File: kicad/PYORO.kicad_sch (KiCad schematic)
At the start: 113 parts, among them J1 BM06B-SRSS-TBLFSN, J2 Conn_01x04_Pin, J3 BM06B-SRSS-TBLFSN, J4 Conn_01x04_Pin, Q1 TEFT4300, Q2 TEFT4300, Q3 TEFT4300, Q4 TEFT4300, Q5 NMOS, Q6 NMOS, Q7 NMOS, Q8 NMOS, Q9 NMOS, SW1 SW_Push_Dual_x2, SW2 SW_Push_Dual_x2, U1 STM32H503CBTx, U10 UCC27524, U3 ICM-20948, U4 MC78LC18NTR, U5 LM1085-5.0, U6 AP2210N-3.3TRG1, U7 UCC27524, U8 ZXMHC3F381N8TC, U9 ZXMHC3F381N8TC

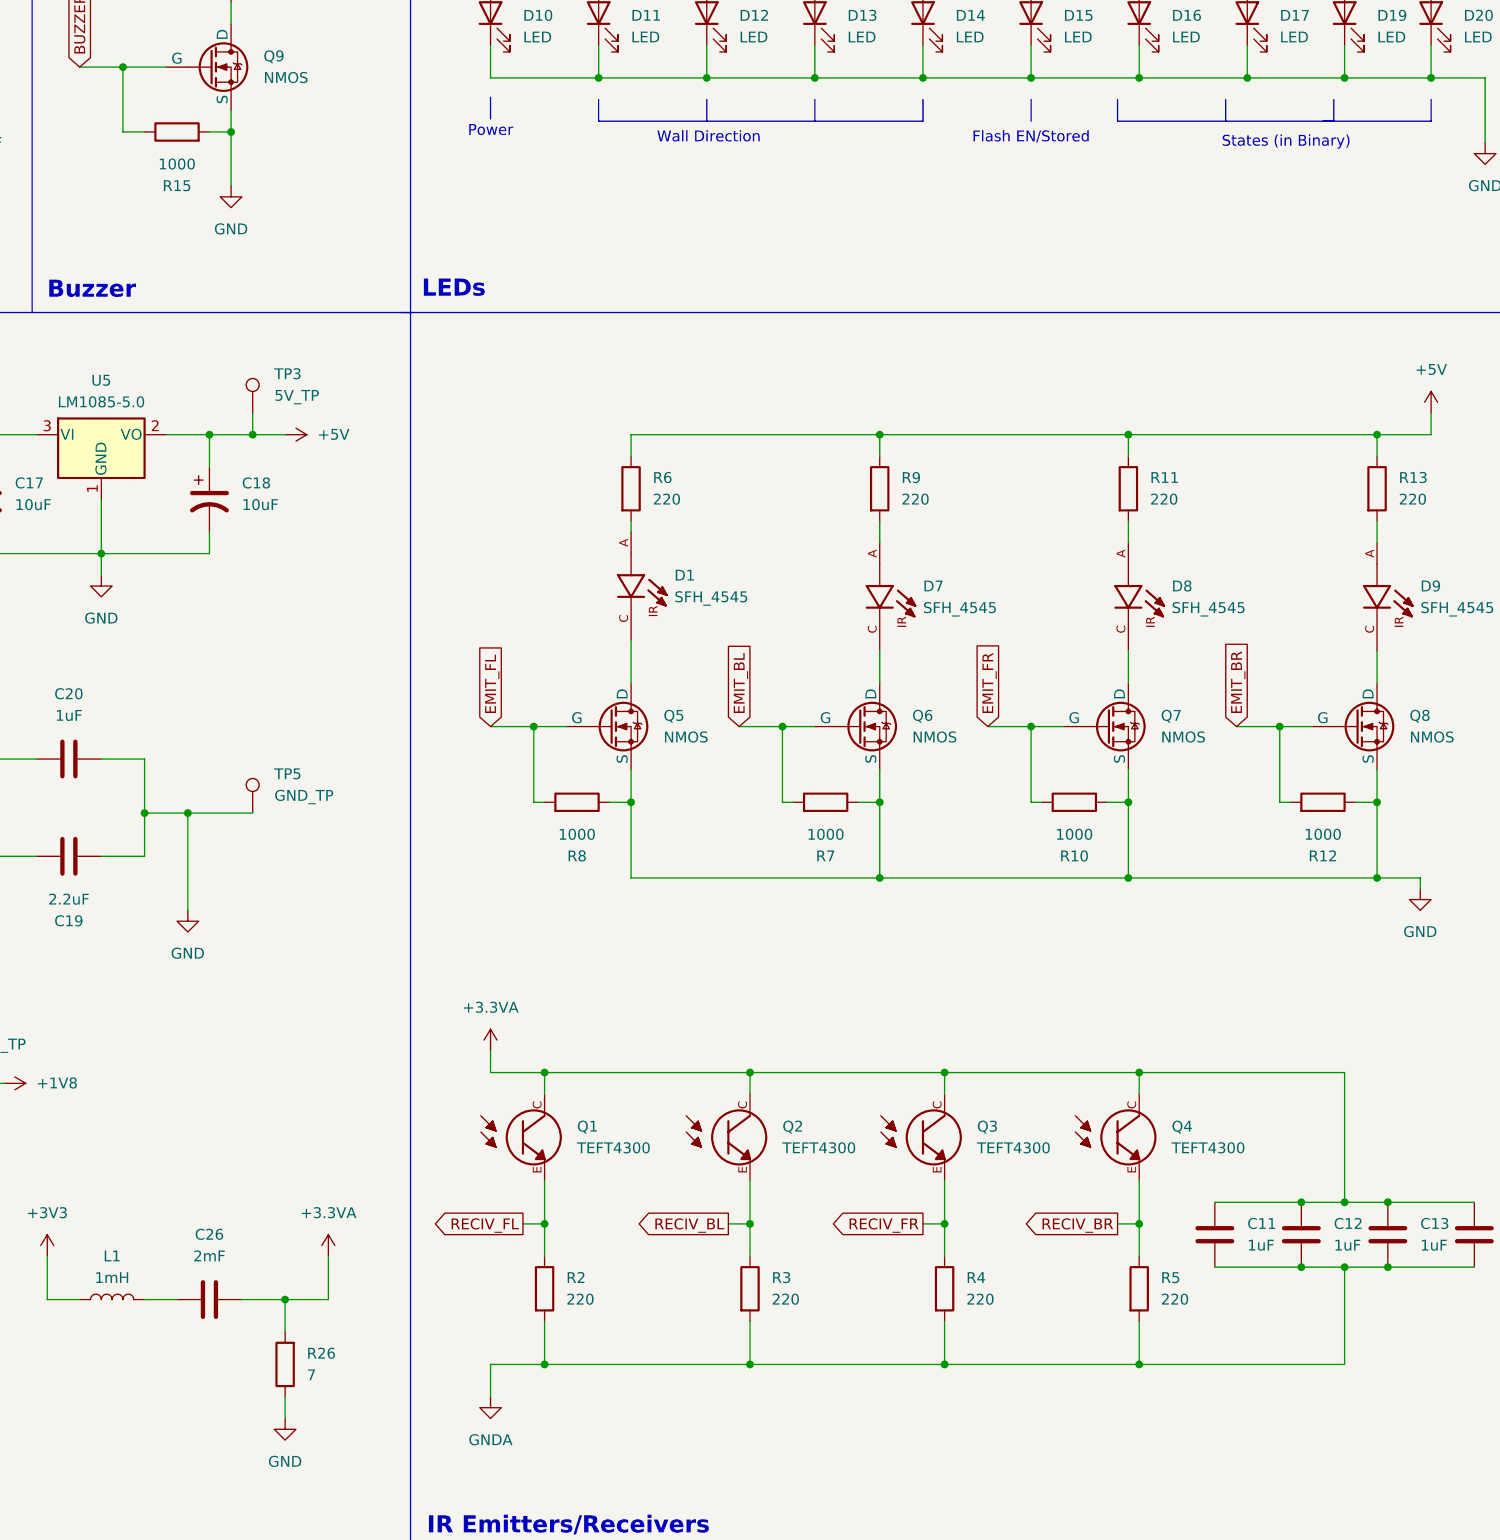
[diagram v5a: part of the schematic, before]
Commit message: Added BOM, and finalized RLC Bandpass filter
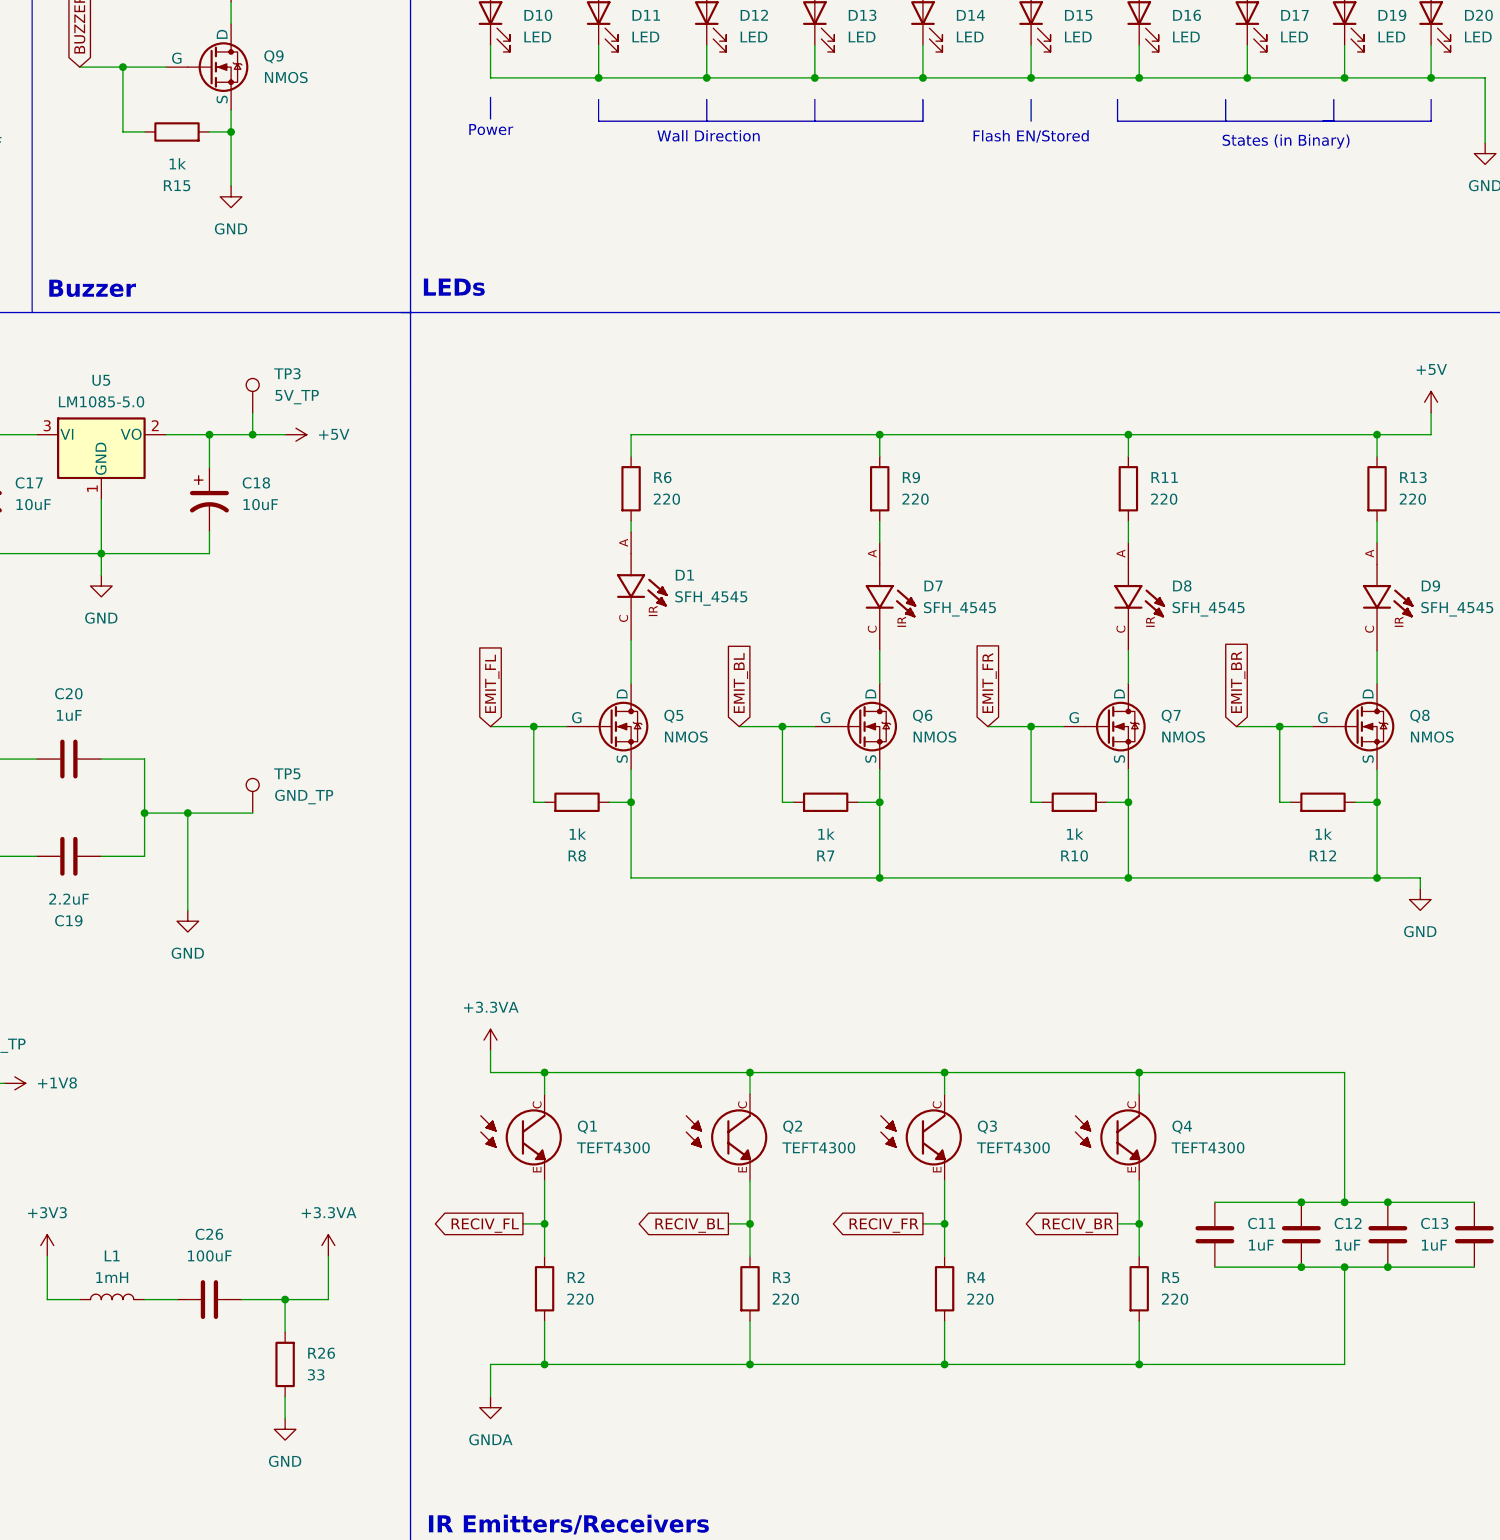
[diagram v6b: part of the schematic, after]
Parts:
- C26: value 2mF -> 100uF
- R10, R12, R15, R7, R8: value 1000 -> 1k
- R26: value 7 -> 33

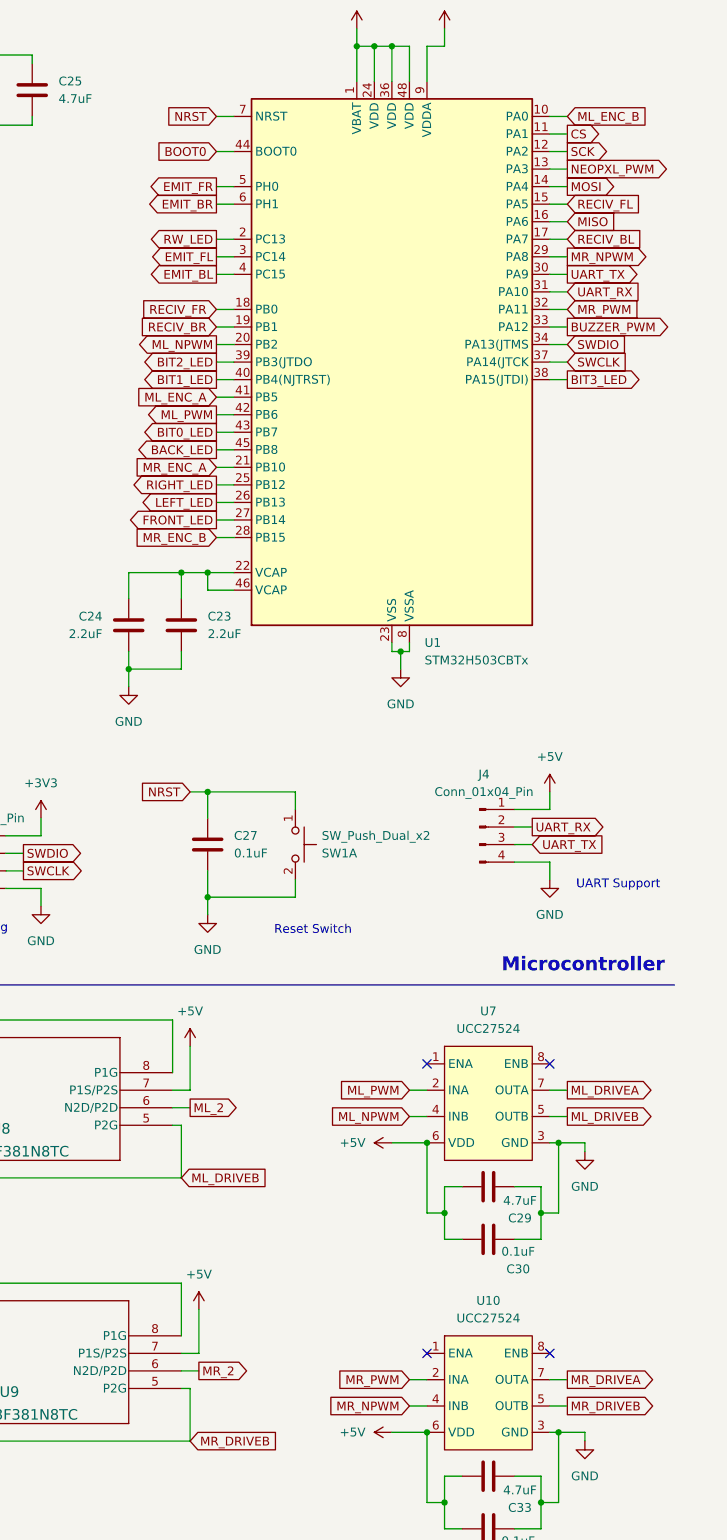
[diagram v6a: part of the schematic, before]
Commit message: Moved all 4 PWM Generations to seperate channels
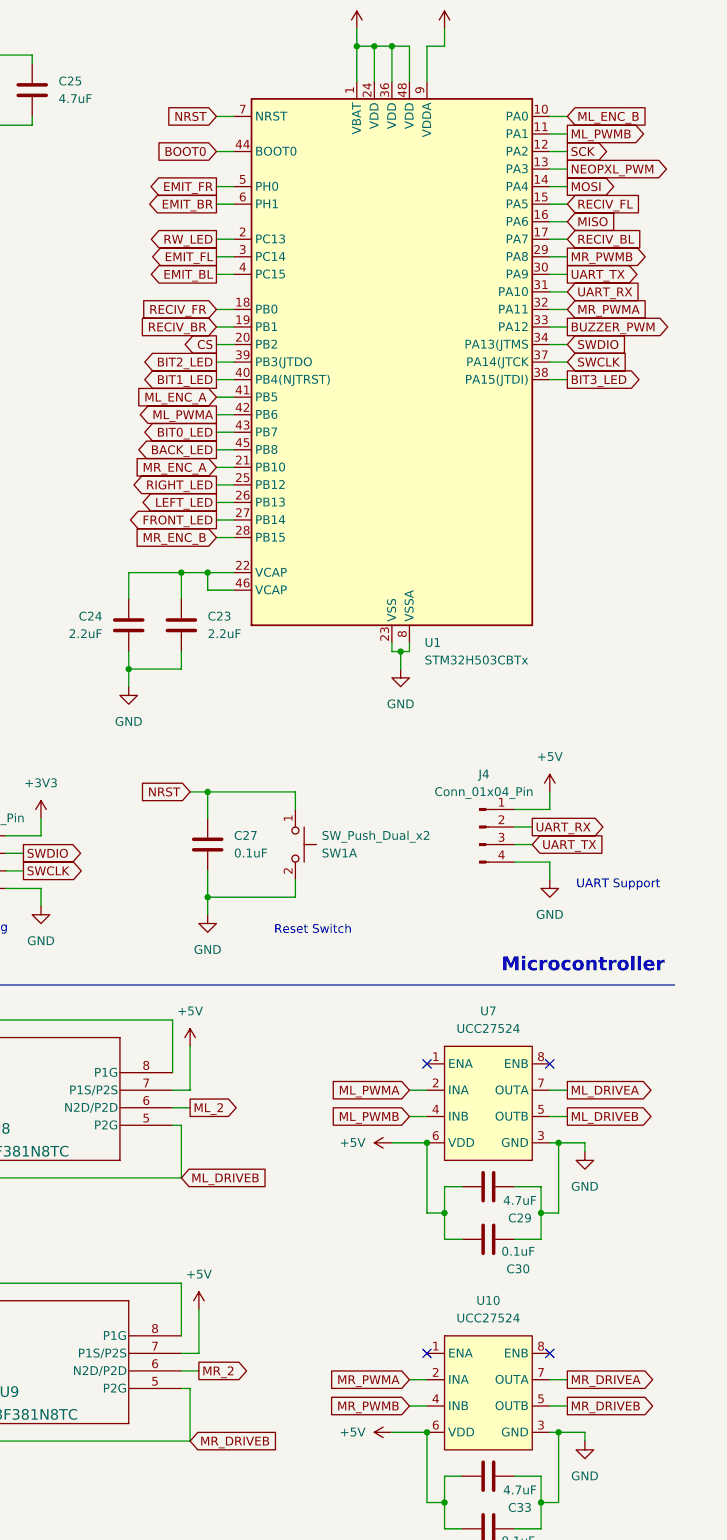
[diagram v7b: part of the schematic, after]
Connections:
- net CS: now also U1.20 (PB2); no longer U1.11 (PA1)
- net ML_NPWM renamed ML_PWMB
- net ML_PWMB: now also U1.11 (PA1); no longer U1.20 (PB2)
- net ML_PWM renamed ML_PWMA
- net MR_NPWM renamed MR_PWMB
- net MR_PWM renamed MR_PWMA

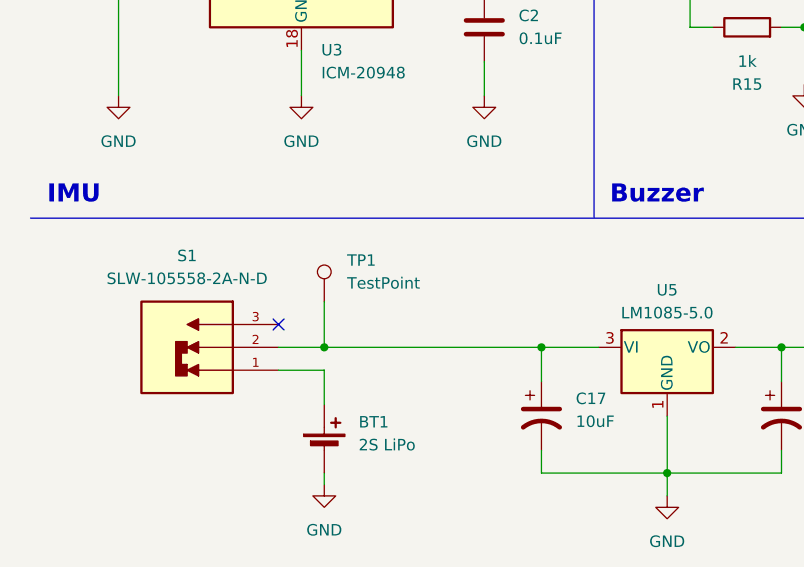
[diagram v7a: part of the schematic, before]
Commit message: Finish importing BOM parts and footprint assignment
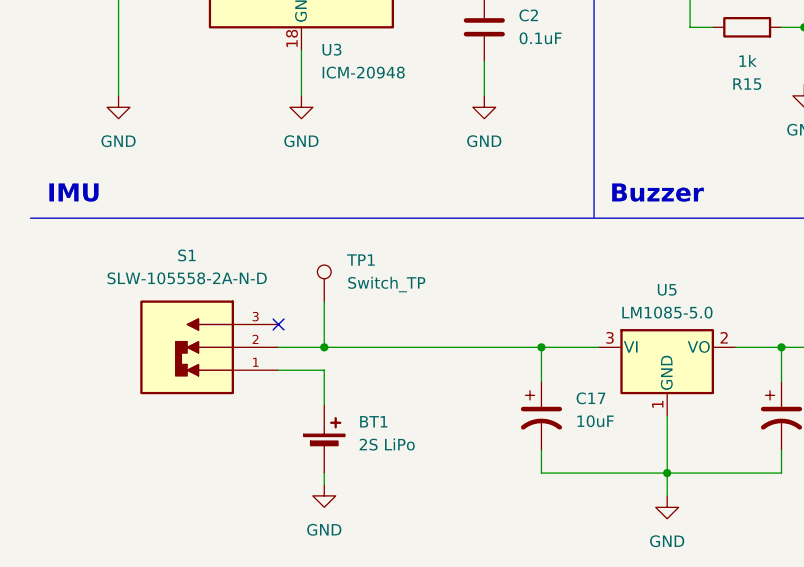
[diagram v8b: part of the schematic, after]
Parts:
- BT1: footprint (none) -> Connector_PinHeader_1.00mm:PinHeader_1x02_P1.00mm_Vertical
- C1, C26, C31, C32: footprint (none) -> Capacitor_THT:CP_Radial_D5.0mm_P2.00mm
- C11, C12, C13, C14, C15, C16, C2, C20, C21, C22, C27, C28, C3, C30, C34, C4, C5, C6, C7, C8: footprint (none) -> Capacitor_SMD:C_1206_3216Metric_Pad1.33x1.80mm_HandSolder
- C17, C18: footprint (none) -> Capacitor_Tantalum_SMD:CP_EIA-3216-18_Kemet-A_Pad1.58x1.35mm_HandSolder
- C19, C23, C24, C25, C29, C33: footprint (none) -> Capacitor_SMD:C_0603_1608Metric_Pad1.08x0.95mm_HandSolder
- D10, D11, D12, D13, D14, D15, D16, D17, D19, D20: footprint (none) -> LED_SMD:LED_1206_3216Metric_Pad1.42x1.75mm_HandSolder
- JP1: footprint (none) -> Jumper:SolderJumper-2_P1.3mm_Bridged_Pad1.0x1.5mm
- L1: footprint (none) -> Inductor_SMD:L_1008_2520Metric_Pad1.43x2.20mm_HandSolder
- Q5, Q6, Q7, Q8, Q9: footprint (none) -> Package_TO_SOT_SMD:SOT-23
- R1, R10, R11, R12, R13, R14, R15, R16, R17, R18, R19, R2, R20, R21, R22, R23, R24, R25, R3, R4, R5, R6, R7, R8, R9: footprint (none) -> Resistor_SMD:R_0603_1608Metric_Pad0.98x0.95mm_HandSolder
- R26: footprint (none) -> Resistor_SMD:R_0805_2012Metric_Pad1.20x1.40mm_HandSolder
- R27: footprint (none) -> Resistor_SMD:R_1206_3216Metric_Pad1.30x1.75mm_HandSolder
- SW1, SW2: footprint (none) -> Button_Switch_SMD:SW_SPST_REED_CT05-XXXX-G1
- TP1: value TestPoint -> Switch_TP; footprint (none) -> Connector_PinHeader_1.00mm:PinHeader_1x01_P1.00mm_Vertical
- TP2, TP3, TP4, TP5: footprint (none) -> Connector_PinHeader_1.00mm:PinHeader_1x01_P1.00mm_Vertical
- U10, U7: footprint (none) -> UCC27524DSDR:DSD8_2P15X1P2
- U5: footprint (none) -> MM_Library:5V Voltage Reg
- U8, U9: footprint SOIC_81N8TC_DIO -> Package_SO:SOIC-8_3.9x4.9mm_P1.27mm
